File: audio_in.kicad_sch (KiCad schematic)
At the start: 26 parts, among them J4 JST SH3, J5 Header_2x1, J6 JST SH3, J7 415-47-208-41-004000, U2 OPA1678

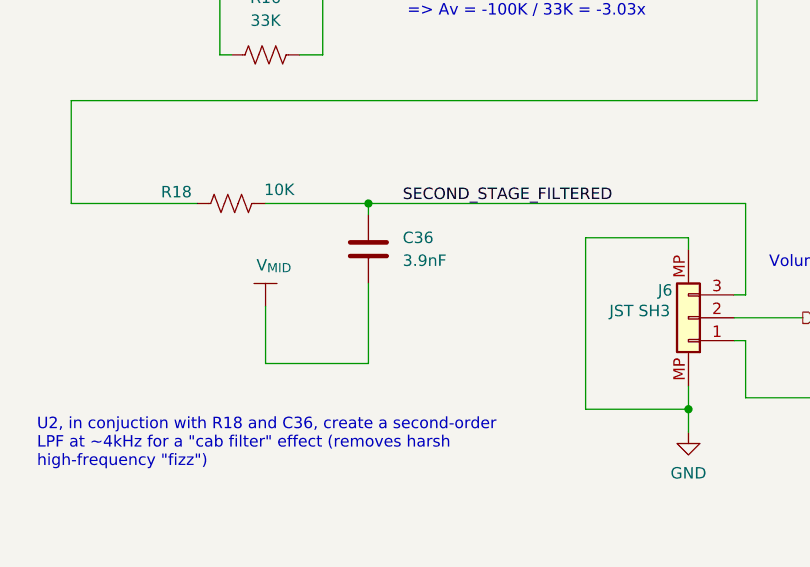
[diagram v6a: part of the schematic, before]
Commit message: Started adding new parts to inventree and re-synchronizing here.
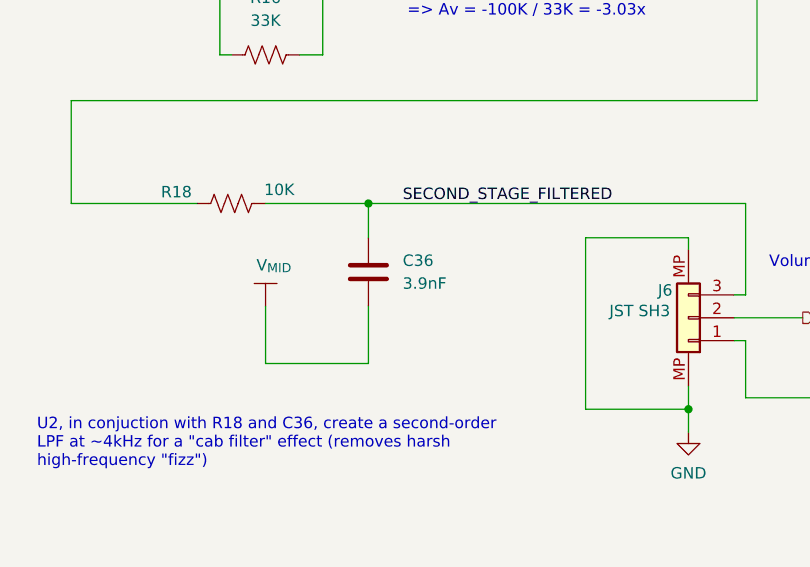
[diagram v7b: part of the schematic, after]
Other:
- moved on the sheet: C36
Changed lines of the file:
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@@
+	)
+	(junction
+		(at 217.17 130.81)
+		(diameter 0)
+		(color 0 0 0 0)
 	)
 	(junction
@@
 	)
 	(junction
-		(at 217.17 130.81)
-		(diameter 0)
-		(color 0 0 0 0)
-	)
-	(junction
 		(at 260.35 100.33)
 		(diameter 0)
@@
 	(wire
 		(pts
-			(xy 217.17 148.59) (xy 217.17 139.7)
+			(xy 217.17 148.59) (xy 217.17 142.24)
 		)
 		(stroke
@@
 	(wire
 		(pts
-			(xy 217.17 130.81) (xy 217.17 132.08)
+			(xy 217.17 130.81) (xy 217.17 134.62)
 		)
 		(stroke
@@
 	(symbol
 		(lib_id "inventree_kicad:C_3900P_NP0_50V_0603")
-		(at 217.17 135.89 0)
+		(at 217.17 138.43 0)
 		(unit 1)
 		(body_style 1)
@@
 		(fields_autoplaced yes)
 		(property "Reference" "C36"
-			(at 220.98 134.6199 0)
+			(at 220.98 137.1599 0)
 			(show_name no)
 			(do_not_autoplace no)
@@
 		)
 		(property "Value" "3.9nF"
-			(at 220.98 137.1599 0)
+			(at 220.98 139.6999 0)
 			(show_name no)
 			(do_not_autoplace no)
@@
 		)
 		(property "Footprint" "Capacitor_SMD:C_0603_1608Metric"
-			(at 218.1352 139.7 0)
+			(at 218.1352 142.24 0)
 			(hide yes)
 			(show_name no)
@@
 		)
 		(property "Datasheet" ""
-			(at 217.17 135.89 0)
+			(at 217.17 138.43 0)
 			(hide yes)
 			(show_name no)
@@
 		)
 		(property "Description" "3900 pF ±5% 50V Ceramic Capacitor C0G, NP0 0603 (1608 Metric)"
-			(at 217.17 135.89 0)
+			(at 217.17 138.43 0)
 			(hide yes)
 			(show_name no)
@@
 		)
 		(property "InvenTree" "30"
-			(at 217.17 135.89 0)
+			(at 217.17 138.43 0)
 			(hide yes)
 			(show_name no)
@@
 		)
 		(property "Part URL" "http://10.0.0.33/web/part/30/"
-			(at 217.17 135.89 0)
+			(at 217.17 138.43 0)
 			(hide yes)
 			(show_name no)
@@
 		)
 		(property "IPN" "301-0011"
-			(at 217.17 135.89 0)
-			(hide yes)
-			(show_name no)
+			(at 217.17 138.43 0)
+			(hide yes)
+			(show_name no)

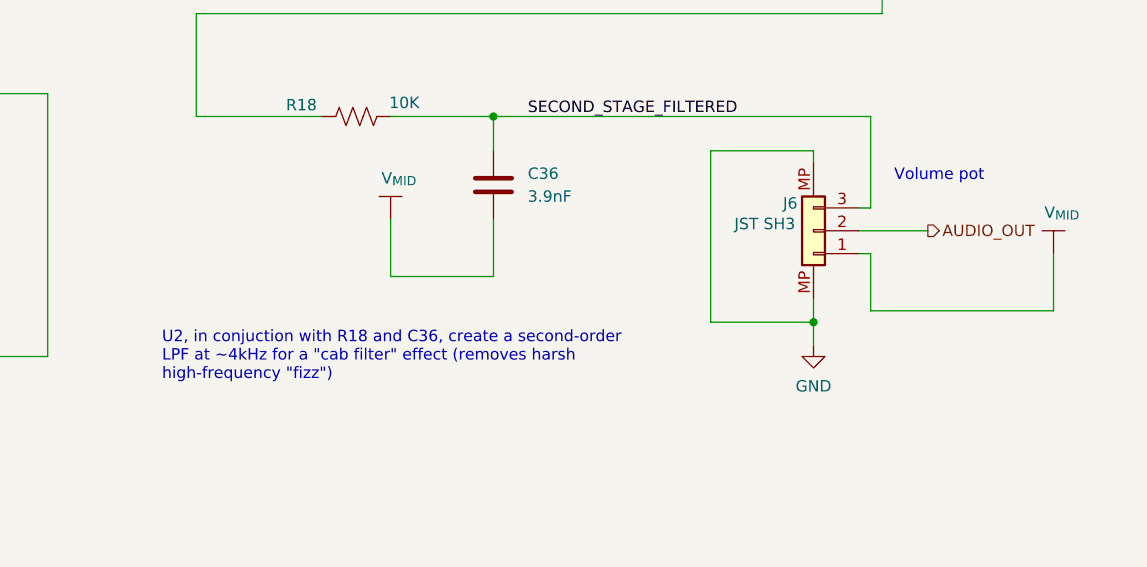
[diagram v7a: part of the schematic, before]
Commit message: Updated theory doc, started layout, fixed a footprint.
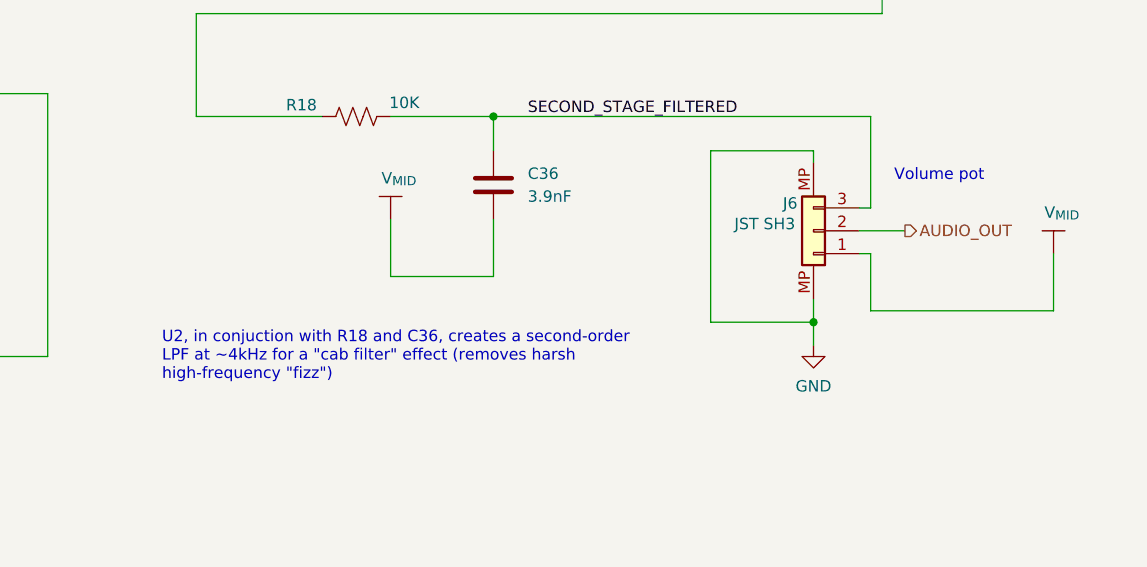
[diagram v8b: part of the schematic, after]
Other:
- note added: "U2, in conjuction with R18 and C36, creates a second-order LPF at ~4kHz for a "cab filter" effect (removes harsh high-frequency "fizz")"
- note removed: "U2, in conjuction with R18 and C36, create a second-order LPF at ~4kHz for a "cab filter" effect (removes harsh high-frequency "fizz")"
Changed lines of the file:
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@@
 		)
 	)
-	(text "U2, in conjuction with R18 and C36, create a second-order\nLPF at ~4kHz for a \"cab filter\" effect (removes harsh\nhigh-frequency \"fizz\")"
+	(text "U2, in conjuction with R18 and C36, creates a second-order\nLPF at ~4kHz for a \"cab filter\" effect (removes harsh\nhigh-frequency \"fizz\")"
 		(exclude_from_sim no)
 		(at 180.34 157.48 0)
@@
 	(wire
 		(pts
-			(xy 257.81 143.51) (xy 265.43 143.51)
+			(xy 257.81 143.51) (xy 262.89 143.51)
 		)
 		(stroke
@@
 	(hierarchical_label "AUDIO_OUT"
 		(shape output)
-		(at 265.43 143.51 0)
-		(effects
-			(font
+		(at 262.89 143.51 0)
+		(effects
+			(font
